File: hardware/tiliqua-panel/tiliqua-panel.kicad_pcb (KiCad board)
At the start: 2 copper layers, 30 x 128.5 mm, 13 parts

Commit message: before panel swap
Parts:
- moved REF** 1.10 mm to (18.4, 15.3)
- moved REF** 1.10 mm to (18.4, 111.8)
- moved REF** 1.10 mm to (13.9, 9.15)
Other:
- outline, holes or cut-outs redrawn

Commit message: after panel swap
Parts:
- added REF**: MountingHole_7.4mm_M6, MountingHole:MountingHole_6.4mm_M6, F.Cu at (7.25, 27.6)
- moved REF** 15.5 mm to (20.0, 111.8)
- moved REF** 15.5 mm to (20.0, 70.4)
- moved REF** 15.5 mm to (20.0, 29.1)
- moved REF** 15.5 mm to (20.0, 84.2)
- moved REF** 15.5 mm to (20.0, 42.9)
- moved REF** 15.5 mm to (20.0, 15.3)
- moved REF** 15.5 mm to (20.0, 98.0)
- moved REF** 15.5 mm to (20.0, 56.7)
- moved REF** 14.8 mm to (14.8, 8.65)
- moved REF** 14.8 mm to (-0.85, 9.00)
- moved REF** 14.7 mm to (3.65, 15.3)
- moved REF** 14.7 mm to (3.65, 111.8)
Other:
- outline, holes or cut-outs redrawn
- board text removed: "A"
- board text removed: "B"
- board text removed: "dbg"
- board text removed: "usr"

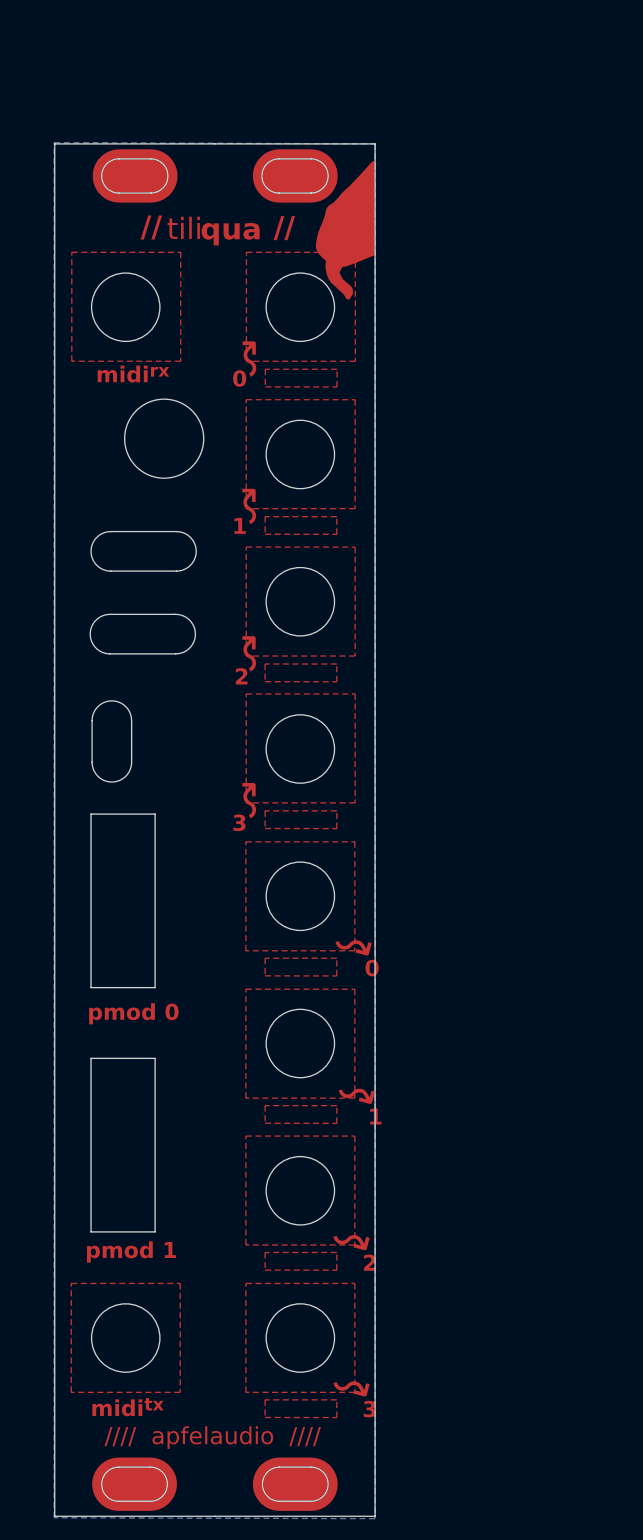
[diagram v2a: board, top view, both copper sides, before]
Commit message: new jack type
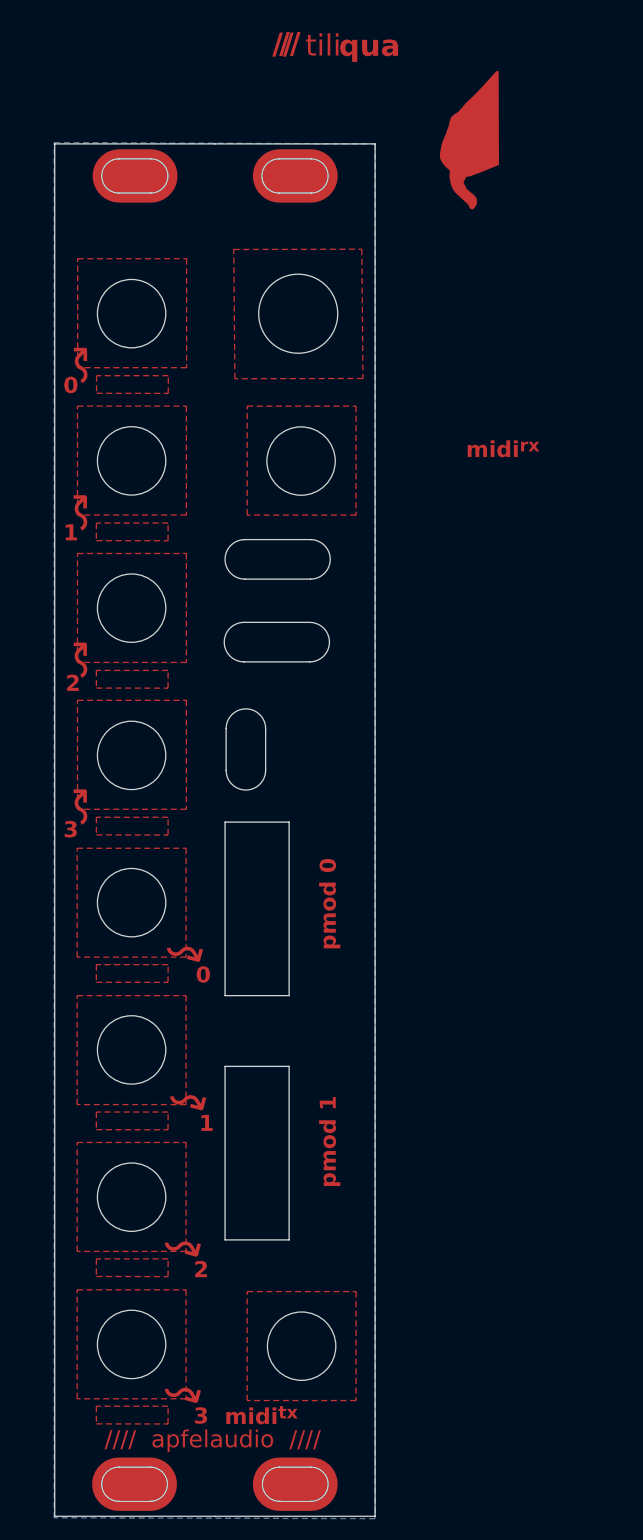
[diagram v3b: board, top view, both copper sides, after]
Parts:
- moved REF** 21.8 mm to (20.1, 29.7)
- moved REF** 17.2 mm to (19.8, 15.9)
- moved REF** 16.5 mm to (20.1, 112.6)
- moved REF** 15.8 mm to (4.20, 112.4)
- moved REF** 15.8 mm to (4.20, 71.0)
- moved REF** 15.8 mm to (4.20, 29.7)
- moved REF** 15.8 mm to (4.20, 84.8)
- moved REF** 15.8 mm to (4.20, 43.5)
- moved REF** 15.8 mm to (4.20, 15.9)
- moved REF** 15.8 mm to (4.20, 98.6)
- moved REF** 15.8 mm to (4.20, 57.3)
- moved REF** 15.7 mm to (-0.80, 8.65)
- moved G*** 14.4 mm to (38.4, -0.94)
- moved REF** 12.6 mm to (11.7, 9.75)
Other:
- outline, holes or cut-outs redrawn

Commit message: check panel look
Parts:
- removed the REF** at (20.1, 29.7)
- moved G*** 86.7 mm to (23.6, 84.5)
- moved REF** 0.28 mm to (20.4, 112.6)
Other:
- outline, holes or cut-outs redrawn
- board text removed: "midi^{tx}"

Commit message: panel jumble
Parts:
- moved G*** 19.0 mm to (26.8, 103.3)
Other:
- board text added: "[apfelaudio]"
- board text added: "control"
- board text added: "debug"
- board text added: "dvi"
- board text added: "ex0"
- board text added: "ex1"
- board text added: "tiliqua"
- board text added: "usb"
- board text removed: "//// apfelaudio ////"
- board text removed: "pmod 0"
- board text removed: "pmod 1"

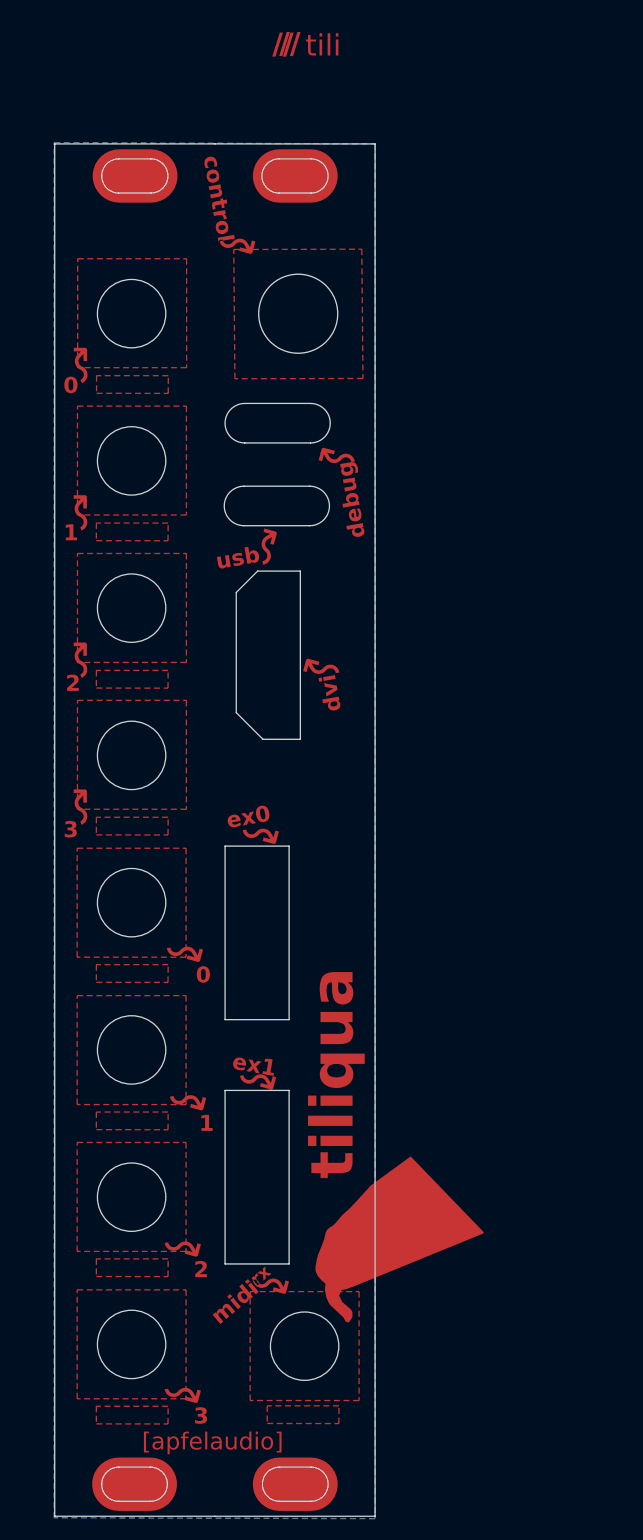
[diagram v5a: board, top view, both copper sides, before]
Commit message: cleaner spacing, align top/bottom parts with pj324
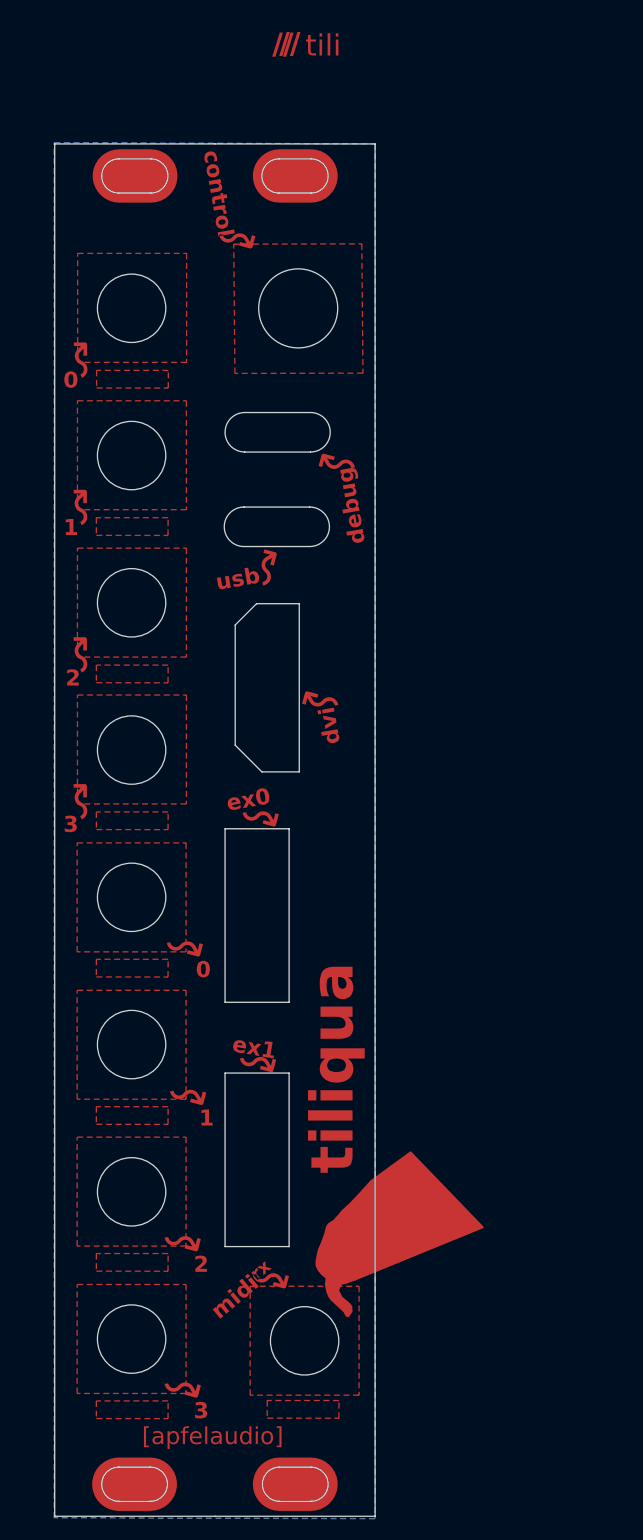
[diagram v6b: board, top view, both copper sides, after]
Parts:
- moved G*** 0.50 mm to (26.8, 102.8)
- moved REF** 0.50 mm to (4.20, 84.3)
- moved REF** 0.50 mm to (4.20, 70.5)
- moved REF** 0.50 mm to (4.20, 29.2)
- moved REF** 0.50 mm to (4.20, 43.0)
- moved REF** 0.50 mm to (20.4, 112.1)
- moved REF** 0.50 mm to (4.20, 15.4)
- moved REF** 0.50 mm to (19.8, 15.4)
- moved REF** 0.50 mm to (4.20, 98.1)
- moved REF** 0.50 mm to (4.20, 56.8)
- moved REF** 0.50 mm to (4.20, 111.9)
- moved REF** 0.25 mm to (11.7, 9.50)
- moved REF** 0.22 mm to (-0.80, 8.88)
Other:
- outline, holes or cut-outs redrawn
